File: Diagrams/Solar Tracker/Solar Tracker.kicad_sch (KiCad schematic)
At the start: 13 parts, among them J1 DS1, J2 M1, J3 M2, J4 MB102

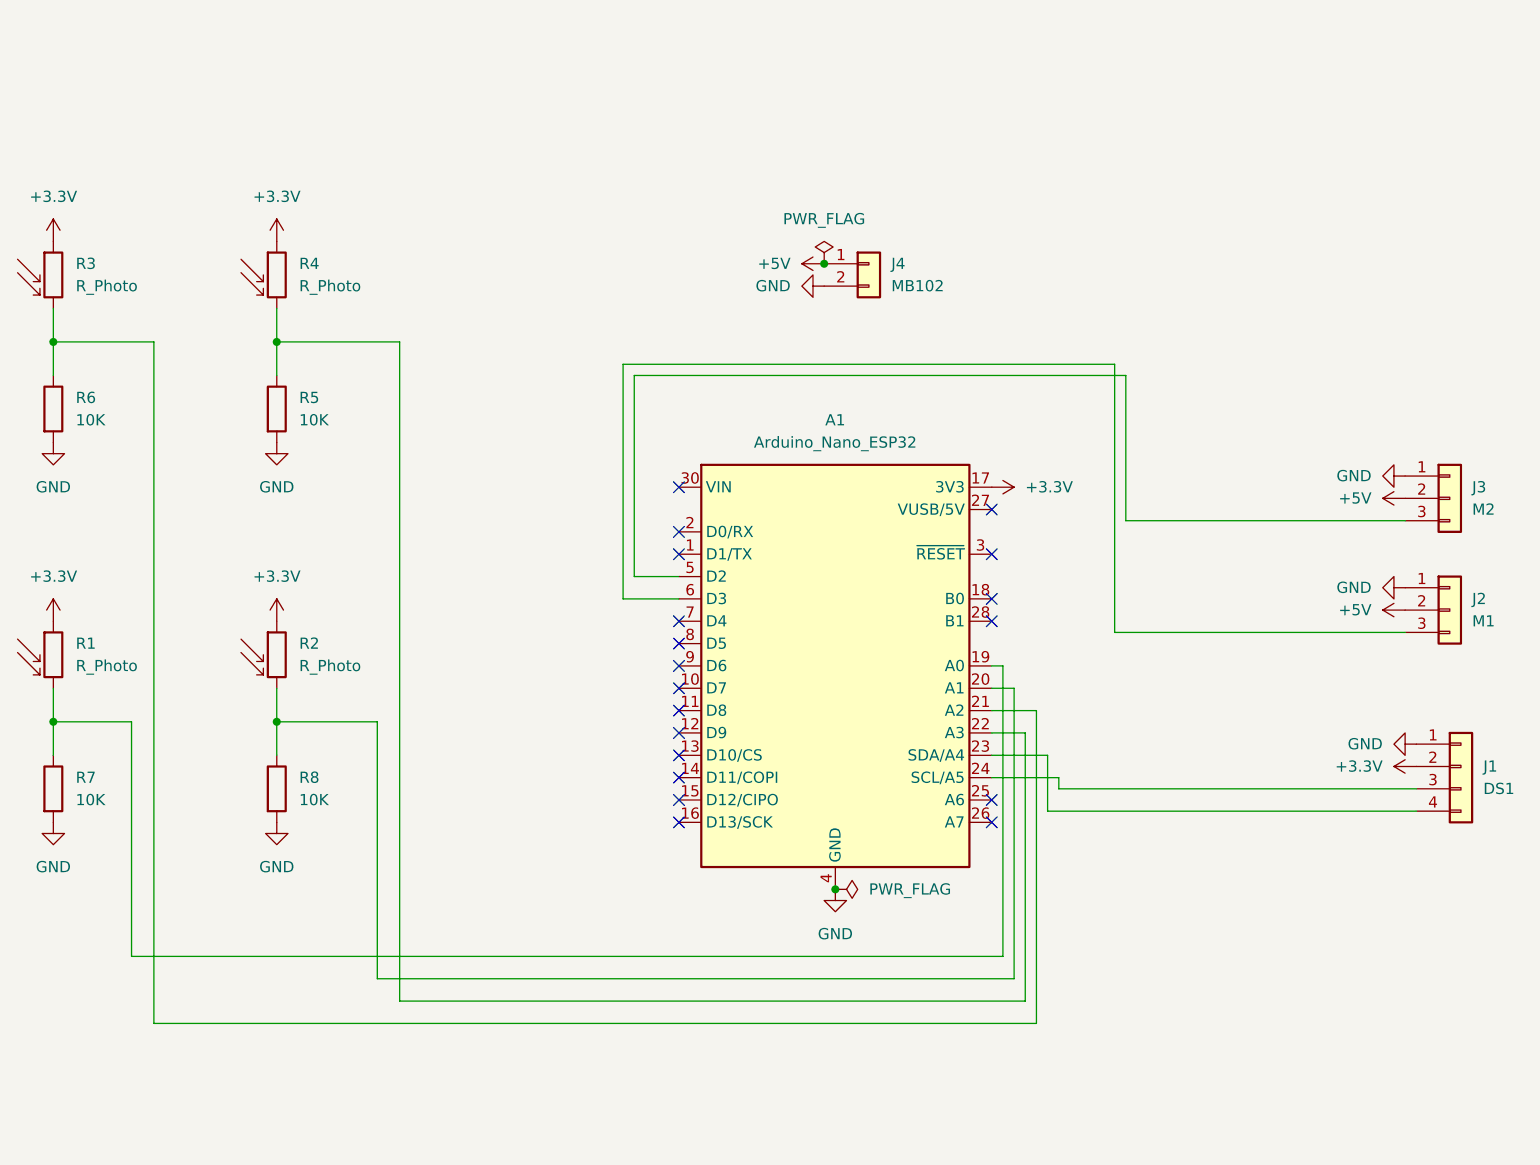
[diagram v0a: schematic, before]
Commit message: Updated the Solar Tracker Schematic
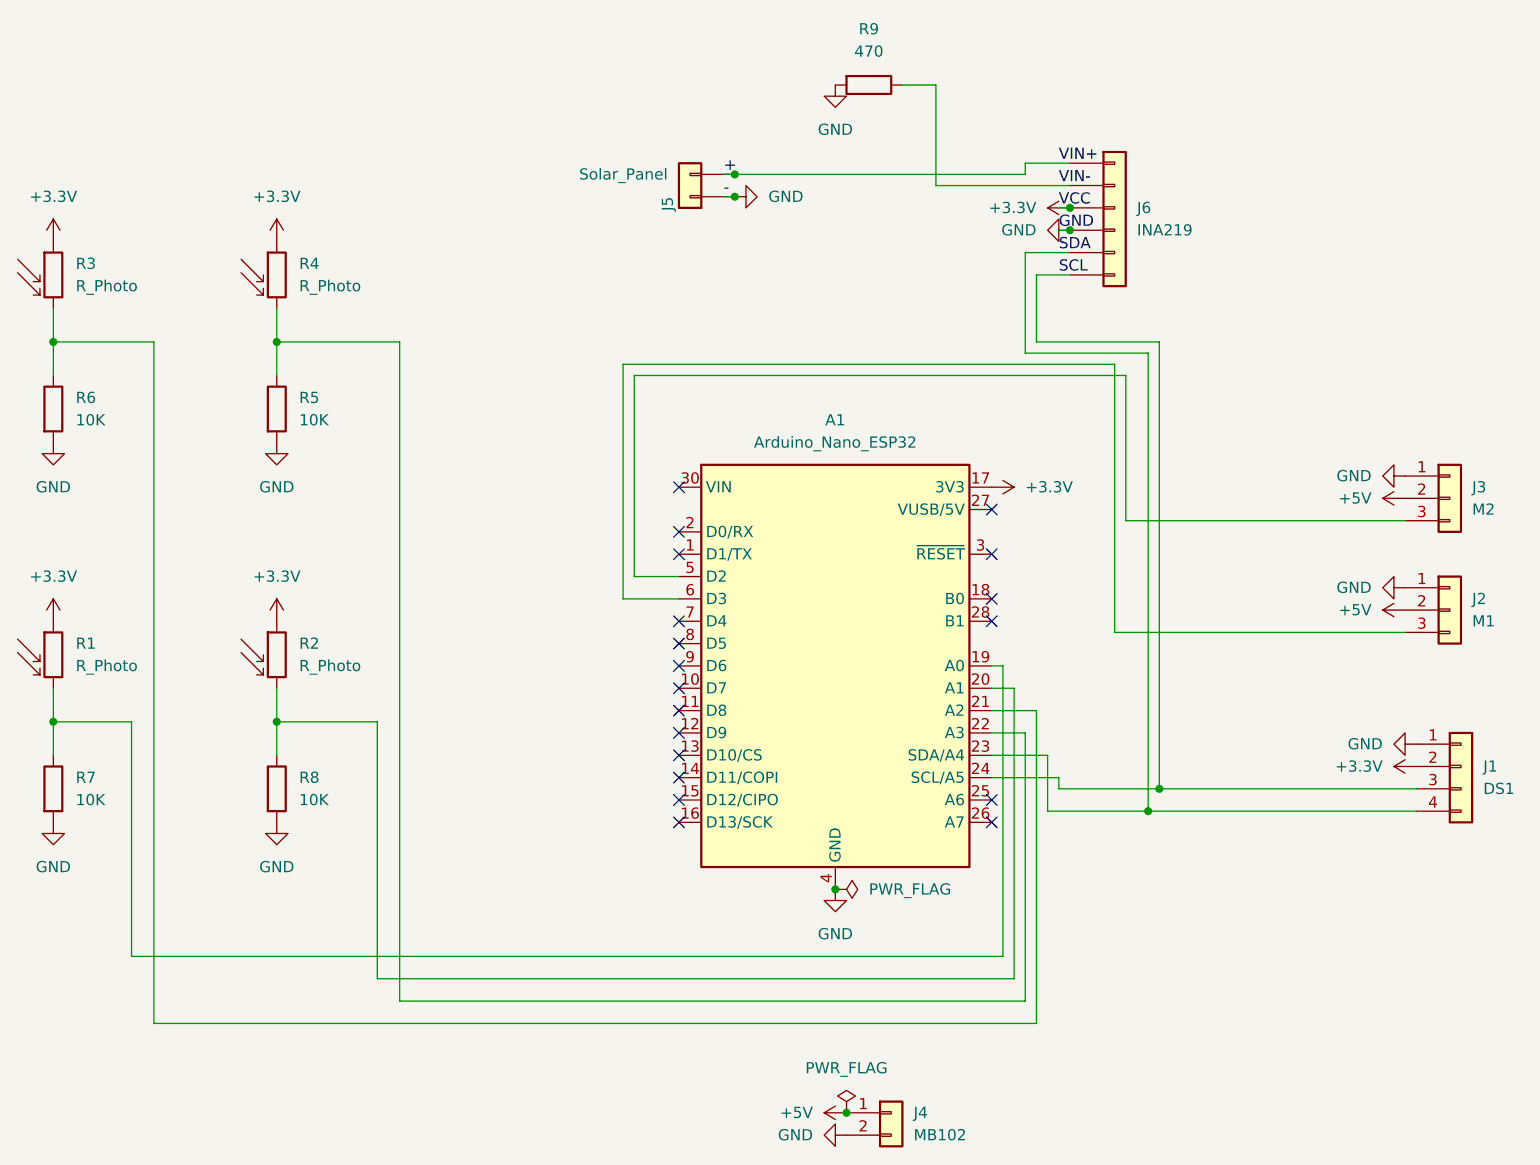
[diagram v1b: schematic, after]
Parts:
- added J5: Solar_Panel, symbol Connector_Generic:Conn_01x02
- added J6: INA219, symbol Connector_Generic:Conn_01x06
- added R9: 470, symbol Device:R
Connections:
- net +3.3V: now also J6.3 (Pin_3)
- net GND: now also J5.1 (Pin_1), J6.4 (Pin_4), R9.2
- net SDA: now reaches A1.23 (SDA/A4), J1.4 (Pin_4)
- net SDA: now also J6.5 (Pin_5)
- net SCL: now reaches A1.24 (SCL/A5), J1.3 (Pin_3)
- net SCL: now also J6.6 (Pin_6)
- new net +: J5.2 (Pin_2), J6.1 (Pin_1)
- new net VIN-: J6.2 (Pin_2), R9.1
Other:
- moved on the sheet: J4

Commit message: Updated SCH file for circuit and Netwired it
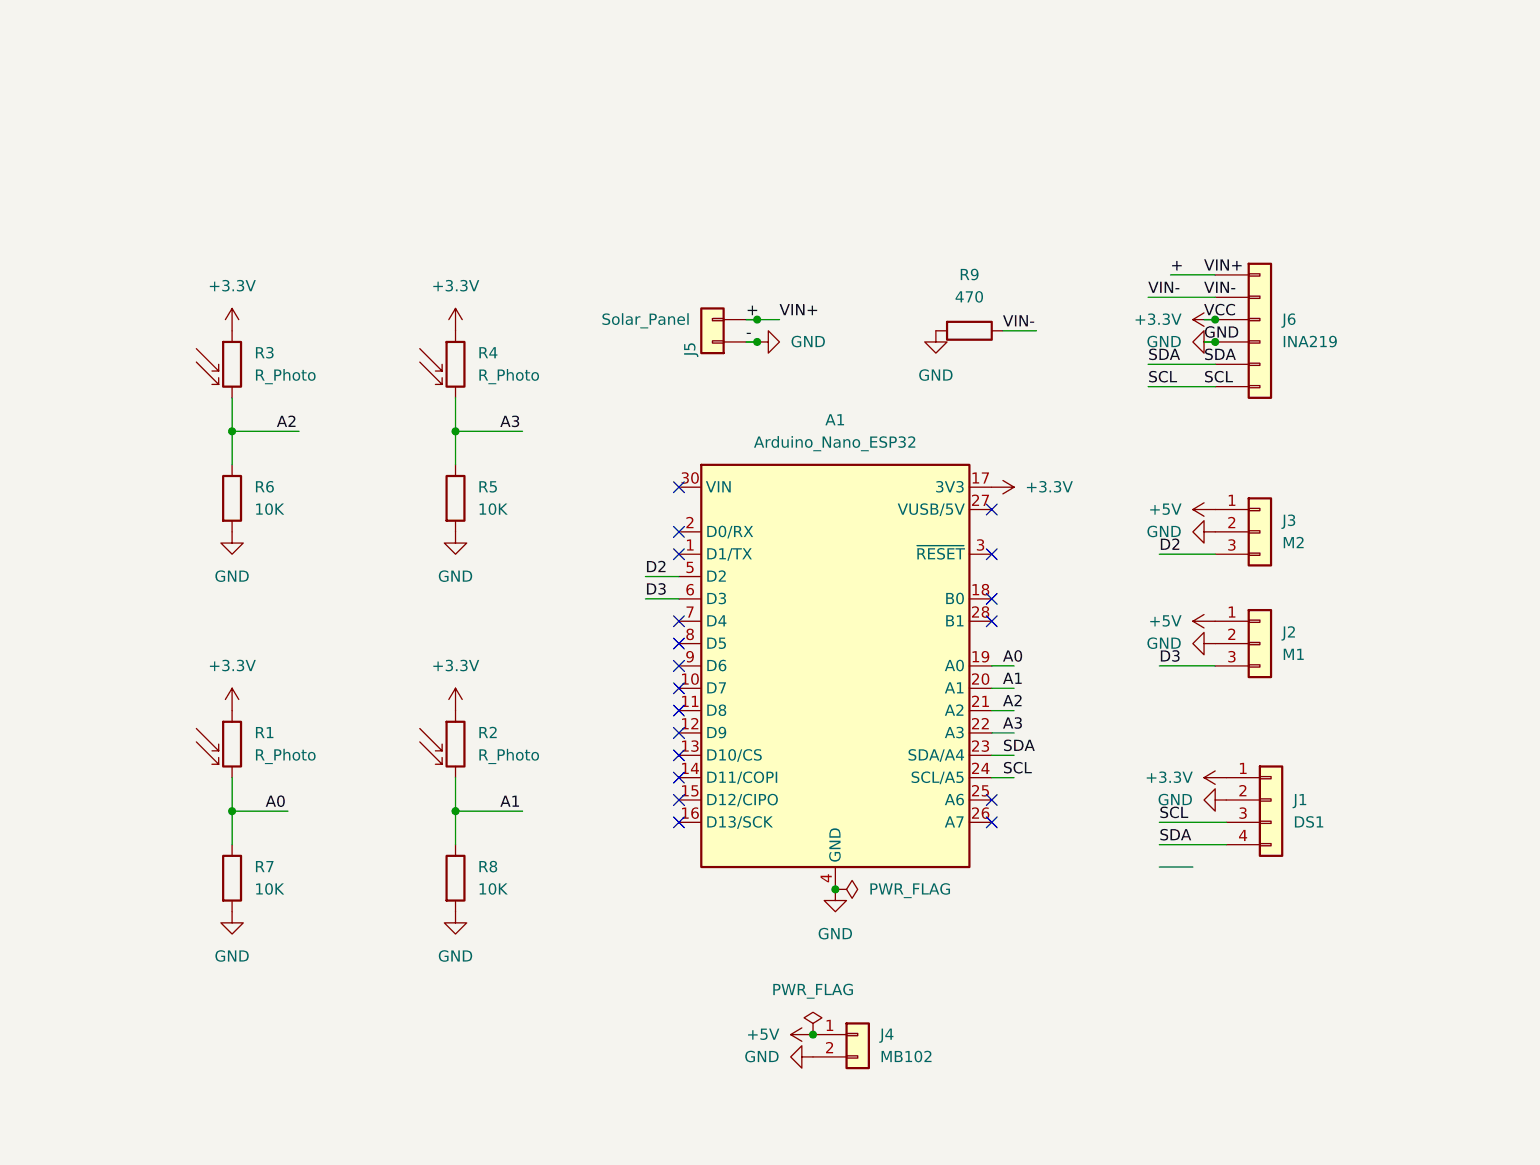
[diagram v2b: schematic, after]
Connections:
- net +3.3V: now also J1.1 (Pin_1); no longer J1.2 (Pin_2)
- net +5V: now also J2.1 (Pin_1), J3.1 (Pin_1); no longer J2.2 (Pin_2), J3.2 (Pin_2)
- net GND: now also J1.2 (Pin_2), J2.2 (Pin_2), J3.2 (Pin_2); no longer J1.1 (Pin_1), J2.1 (Pin_1), J3.1 (Pin_1)
- net A3: now reaches A1.22 (A3), R4.2, R5.1
- net D2: now reaches A1.5 (D2), J3.3 (Pin_3)
- net A0: now reaches A1.19 (A0), R1.2, R7.1
- net A1: now reaches A1.20 (A1), R2.2, R8.1
- net A2: now reaches A1.21 (A2), R3.2, R6.1
- net D3: now reaches A1.6 (D3), J2.3 (Pin_3)
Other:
- moved on the sheet: J1, J2, J3, J4, J5, J6, R1, R2, R3, R4, R5, R6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

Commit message: Update Solar Tracker schematic & project files
Add updated screen module PDF and apply multiple KiCad project/schematic updates. Changes include updating used_designators in the .kicad_pro, adding a generic 1x08 connector symbol and many schematic edits (repositioned junctions, wires and labels, removed/adjusted no_connect items and updated UUIDs) in Solar Tracker.kicad_sch, and removing a stale .kicad_pro lock. Also include small project changes to platformio.ini and src/main.cpp.
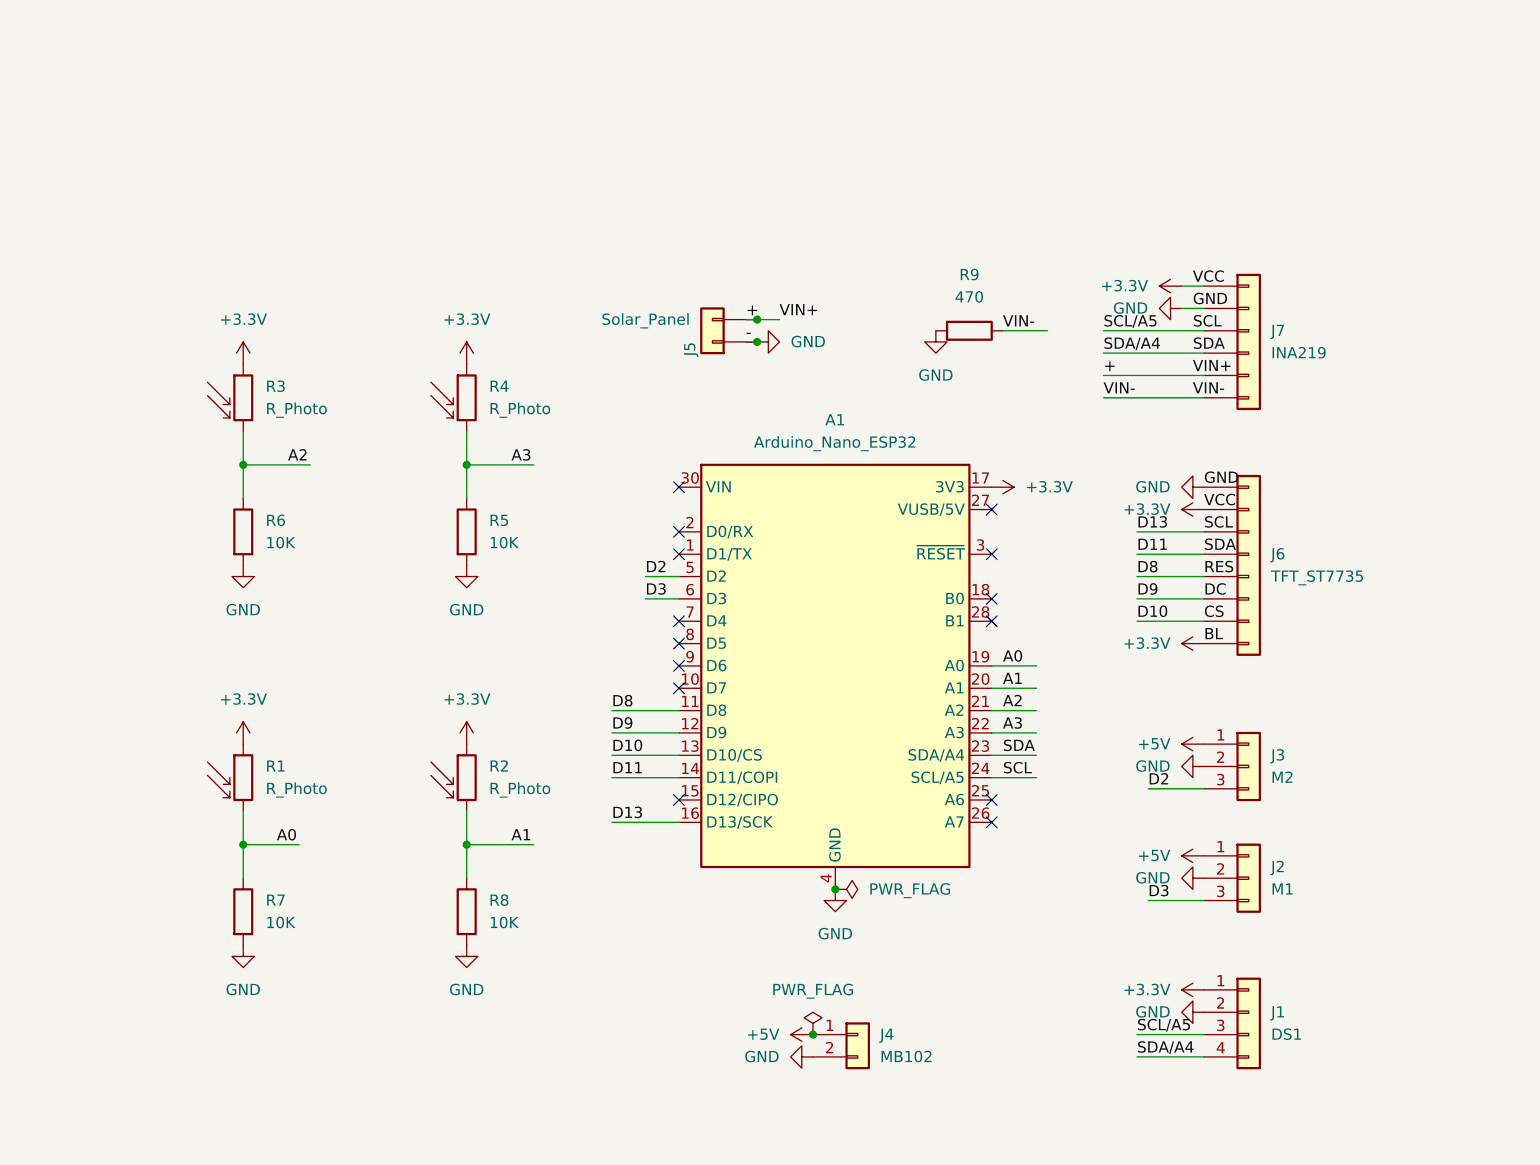
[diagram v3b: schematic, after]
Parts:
- removed J6: INA219, symbol Connector_Generic:Conn_01x06
- added J6: TFT_ST7735, symbol Connector_Generic:Conn_01x08
- added J7: INA219, symbol Connector_Generic:Conn_01x06
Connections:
- net SCL is gone; now on net D13: A1.24 (SCL/A5), J1.3 (Pin_3)
- net SDA is gone; now on net D11: A1.23 (SDA/A4), J1.4 (Pin_4)
- net +: now also J7.5 (Pin_5)
- net +3.3V: now also J6.2 (Pin_2), J6.8 (Pin_8), J7.1 (Pin_1)
- net GND: now also J6.1 (Pin_1), J7.2 (Pin_2)
- net VIN-: now also J7.6 (Pin_6)
- net D8: now reaches A1.11 (D8)
- net D8: now also J6.5 (Pin_5)
- net D9: now reaches A1.12 (D9)
- net D9: now also J6.6 (Pin_6)
- net CS: now reaches A1.13 (D10/CS)
- net CS: now also J6.7 (Pin_7)
- net D11: now reaches A1.14 (D11/COPI)
- net D11: now also J6.4 (Pin_4), J7.4 (Pin_4)
- net D13: now reaches A1.16 (D13/SCK)
- net D13: now also J6.3 (Pin_3), J7.3 (Pin_3)
- no-connect marks 19 -> 14
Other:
- moved on the sheet: J1, J2, J3, R1, R2, R3, R4, R5, R6, R7, R8
